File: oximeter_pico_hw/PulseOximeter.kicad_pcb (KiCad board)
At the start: 2 copper layers, 95 x 79 mm, 28 parts, among them Q1 IRLML2060, Q2 IRLML2060, Q3 IRLML2060, Q4 IRLML2060, Q5 IRLML2060, Q6 IRLML2060, Q7 IRLML2060, U1 Pico, U2 SFH7060, U3 DC56-11YWA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

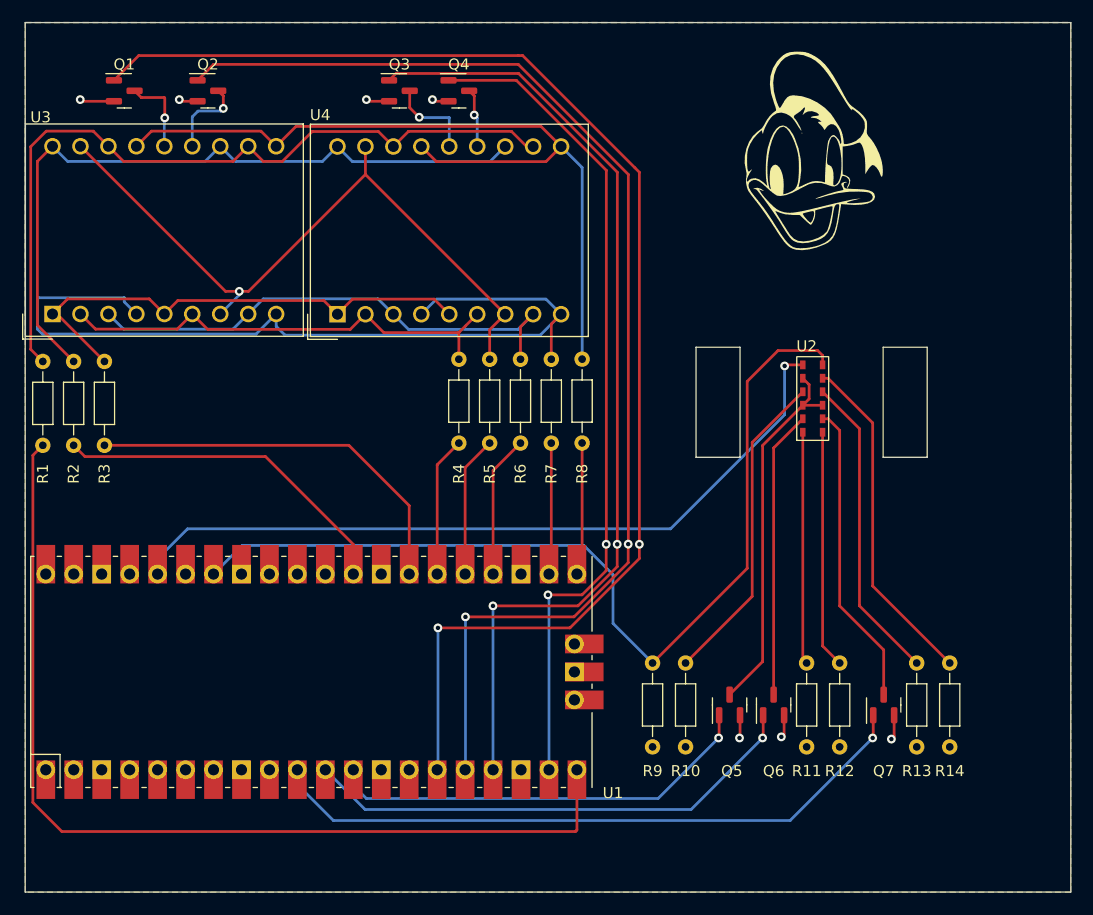
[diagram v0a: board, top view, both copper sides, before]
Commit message: Update HW to revision 2
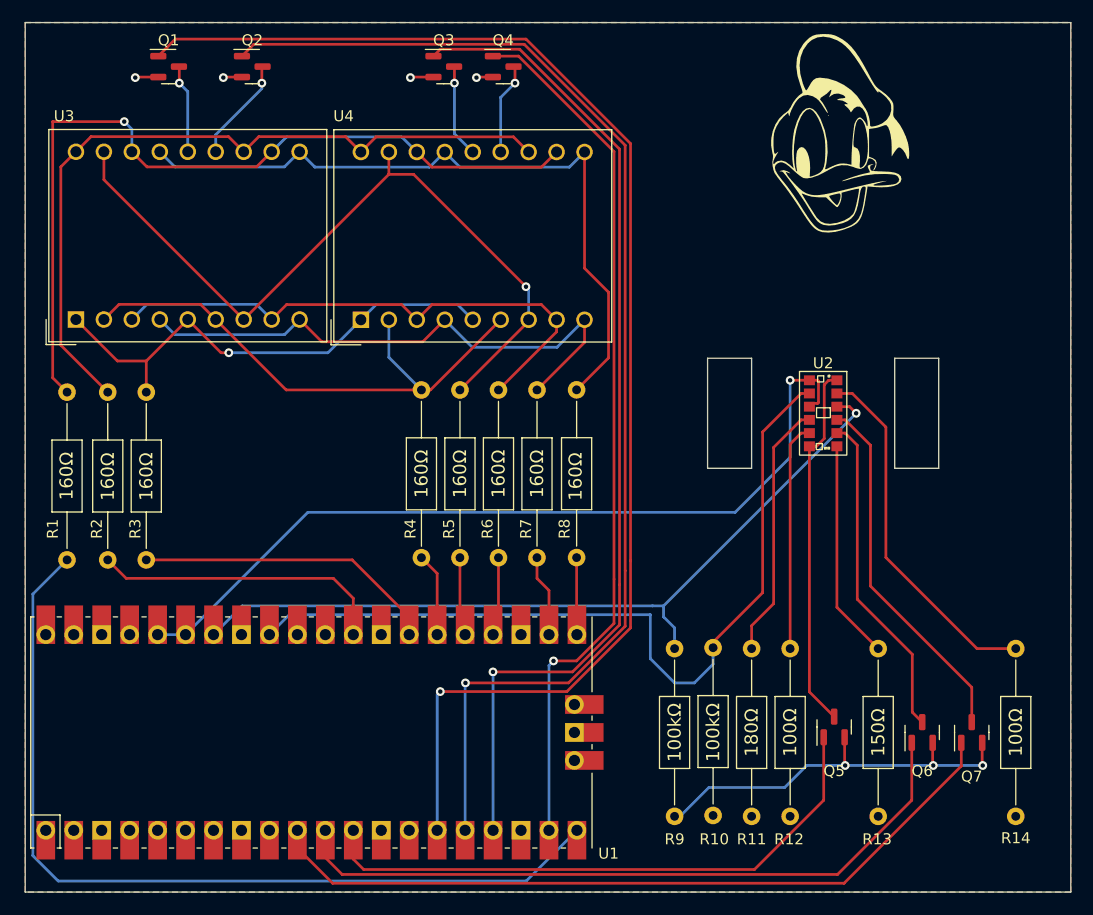
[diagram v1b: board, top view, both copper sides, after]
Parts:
- R1, R11, R2, R3, R4, R5, R6, R7, R8, R9: footprint Resistor_THT:R_Axial_DIN0204_L3.6mm_D1.6mm_P7.62mm_Horizontal -> Resistor_THT:R_Axial_DIN0207_L6.3mm_D2.5mm_P15.24mm_Horizontal
- R10: value 91 -> 100k; footprint Resistor_THT:R_Axial_DIN0204_L3.6mm_D1.6mm_P7.62mm_Horizontal -> Resistor_THT:R_Axial_DIN0207_L6.3mm_D2.5mm_P15.24mm_Horizontal
- R12: value 150 -> 100; footprint Resistor_THT:R_Axial_DIN0204_L3.6mm_D1.6mm_P7.62mm_Horizontal -> Resistor_THT:R_Axial_DIN0207_L6.3mm_D2.5mm_P15.24mm_Horizontal
- R13: value 91 -> 150; footprint Resistor_THT:R_Axial_DIN0204_L3.6mm_D1.6mm_P7.62mm_Horizontal -> Resistor_THT:R_Axial_DIN0207_L6.3mm_D2.5mm_P15.24mm_Horizontal
- R14: value 91 -> 100; footprint Resistor_THT:R_Axial_DIN0204_L3.6mm_D1.6mm_P7.62mm_Horizontal -> Resistor_THT:R_Axial_DIN0207_L6.3mm_D2.5mm_P15.24mm_Horizontal
- U2: value SFH7060 -> SFH7072; footprint OptoDevice:SFH7060 -> OptoDevice:SFH7072
- moved Q7 18.2 mm to (163.0, 122.5)
- moved R11 14.8 mm to (143.0, 130.1), turned to 90 degrees
- moved R12 14.6 mm to (146.5, 130.1), turned to 90 degrees
- moved R3 11.1 mm to (88.0, 106.8)
- moved R4 11.0 mm to (113.0, 106.6)
- moved R2 10.9 mm to (84.5, 106.8)
- moved R5 10.8 mm to (116.5, 106.6)
- moved R1 10.6 mm to (80.8, 106.8)
- moved R6 10.6 mm to (120.0, 106.6)
- moved R7 10.5 mm to (123.5, 106.6)
- moved R8 10.4 mm to (127.1, 106.6)
- moved Q5 9.71 mm to (150.5, 122.0)
- moved R10 9.35 mm to (139.5, 114.8), turned to -90 degrees
- moved R14 8.71 mm to (167.0, 130.1)
- moved R13 7.22 mm to (154.5, 130.1)
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- renumbered Q7 to Q6, Q6 to Q7
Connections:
- R10 pad 1: +5V -> PHOTOTR_BB
- R10 pad 2: Net-(R10-Pad2) -> GND
- R11 pad 1: Net-(R11-Pad1) -> +5V
- R11 pad 2: +5V -> Net-(R11-Pad2)
- R12 pad 1: Net-(R12-Pad1) -> +5V
- R12 pad 2: +5V -> Net-(R12-Pad2)
- R9 pad 1: PHOTOTR -> PHOTOTR_IR
- U1 pad 10: TR_R -> TR_I
- U1 pad 11: TR_I -> TR_R
- U1 pad 32: unconnected-(U1-Pad32) -> PHOTOTR_BB
- U1 pad 34: PHOTOTR -> PHOTOTR_IR
- U1 pad 35: unconnected-(U1-Pad35) -> +3V3
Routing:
- net PHOTOTR: track 86.2 -> 0.00 mm
- net PHOTOTR_BB: track 0.00 -> 75.3 mm
- net PHOTOTR_IR: track 0.00 -> 73.0 mm, vias 0 -> 1
- net /DP: track 81.7 -> 51.6 mm
- net GND: track 14.9 -> 44.3 mm
- net Net-(R10-Pad2): track 29.1 -> 0.00 mm
- net TR_I: track 46.0 -> 69.8 mm, vias 1 -> 0
- net Net-(R11-Pad2): track 0.00 -> 23.4 mm
- net Net-(R12-Pad1): track 21.6 -> 0.00 mm
- net Net-(R11-Pad1): track 21.1 -> 0.00 mm
- net Net-(R12-Pad2): track 0.00 -> 20.7 mm
- net TR_G: track 40.0 -> 54.1 mm, vias 1 -> 0
- net /B: track 75.2 -> 65.7 mm
- net SEG_E: track 36.2 -> 27.6 mm
- net SEG_A: track 88.9 -> 80.5 mm
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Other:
- outline, holes or cut-outs redrawn
- board text added: "100kΩ"
- board text added: "100Ω"
- board text added: "150Ω"
- board text added: "160Ω"
- board text added: "180Ω"
- board text added: "JLCJLCJLCJLC"
